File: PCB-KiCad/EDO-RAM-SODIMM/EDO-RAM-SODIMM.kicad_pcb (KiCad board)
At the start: 2 copper layers, 1 part

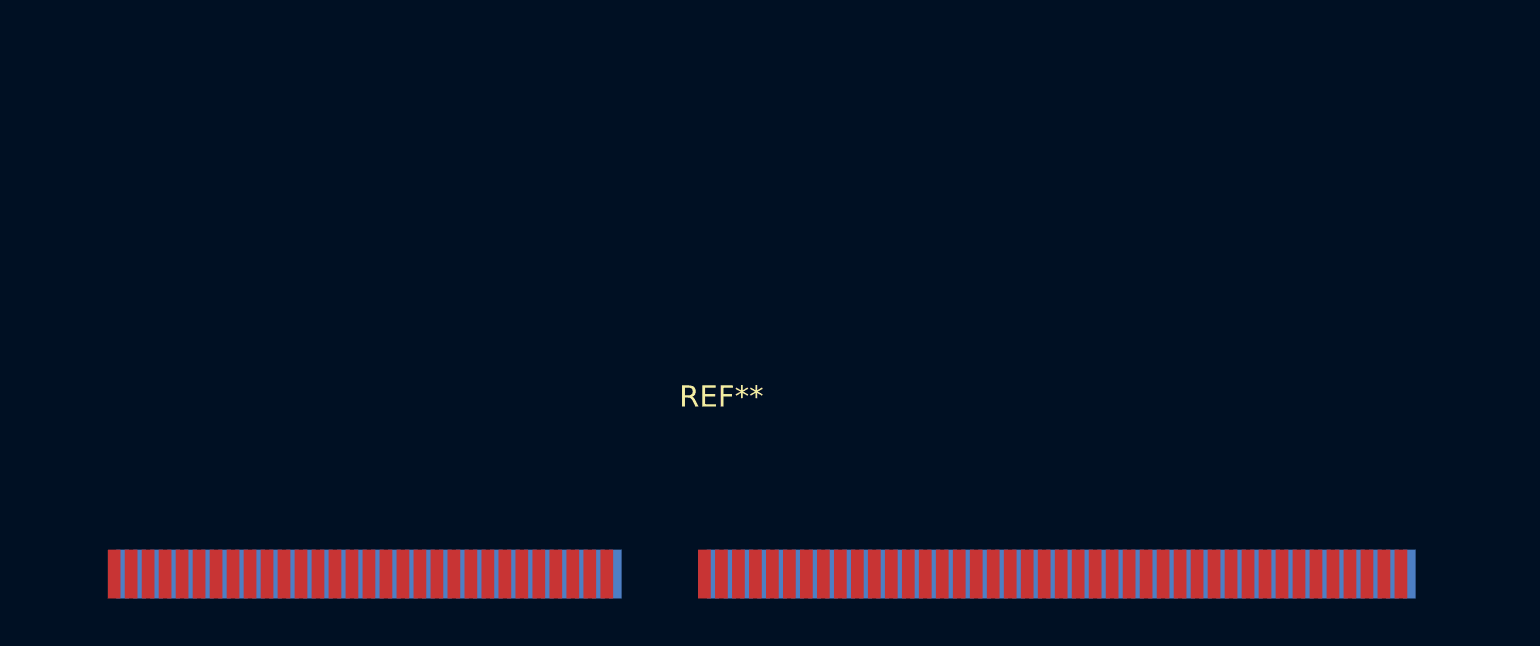
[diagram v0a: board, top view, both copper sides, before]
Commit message: U1 Connections
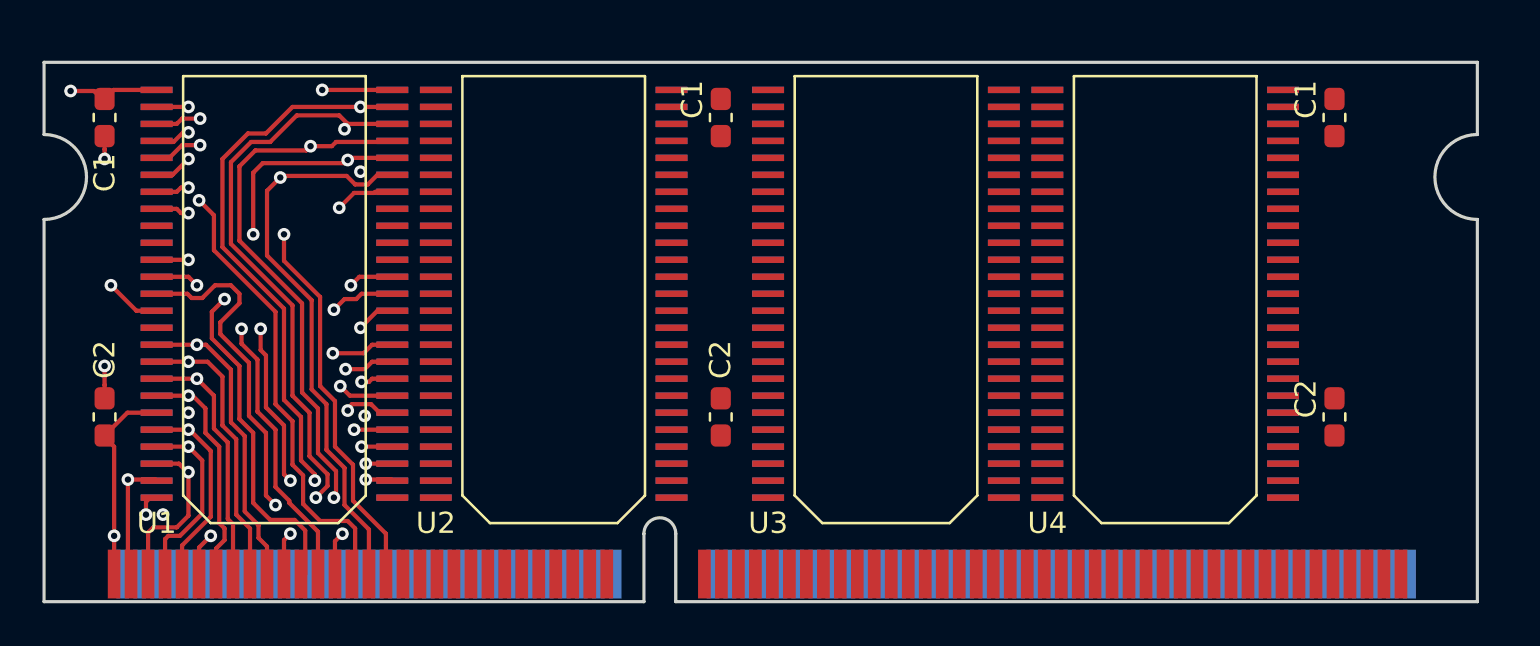
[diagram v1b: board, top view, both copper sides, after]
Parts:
- added C1: C_0603_1608Metric_Pad1.05x0.95mm_HandSolder, Capacitor_SMD:C_0603_1608Metric_Pad1.05x0.95mm_HandSolder, F.Cu at (150.4, 84.8)
- added C1: C_0603_1608Metric_Pad1.05x0.95mm_HandSolder, Capacitor_SMD:C_0603_1608Metric_Pad1.05x0.95mm_HandSolder, F.Cu at (121.5, 84.8)
- added C1: C_0603_1608Metric_Pad1.05x0.95mm_HandSolder, Capacitor_SMD:C_0603_1608Metric_Pad1.05x0.95mm_HandSolder, F.Cu at (92.5, 84.8)
- added C2: C_0603_1608Metric_Pad1.05x0.95mm_HandSolder, Capacitor_SMD:C_0603_1608Metric_Pad1.05x0.95mm_HandSolder, F.Cu at (150.4, 98.8)
- added C2: C_0603_1608Metric_Pad1.05x0.95mm_HandSolder, Capacitor_SMD:C_0603_1608Metric_Pad1.05x0.95mm_HandSolder, F.Cu at (121.5, 98.8)
- added C2: C_0603_1608Metric_Pad1.05x0.95mm_HandSolder, Capacitor_SMD:C_0603_1608Metric_Pad1.05x0.95mm_HandSolder, F.Cu at (92.5, 98.8)
- added U1: SOIC-50, obsolete-chips:SOIC-50, B.Cu at (100.7, 93.0)
- added U1: SOIC-50, obsolete-chips:SOIC-50, F.Cu at (100.7, 93.0)
- added U2: SOIC-50, obsolete-chips:SOIC-50, B.Cu at (113.8, 93.0)
- added U2: SOIC-50, obsolete-chips:SOIC-50, F.Cu at (113.8, 93.0)
- added U3: SOIC-50, obsolete-chips:SOIC-50, B.Cu at (129.5, 93.0)
- added U3: SOIC-50, obsolete-chips:SOIC-50, F.Cu at (129.5, 93.0)
- added U4: SOIC-50, obsolete-chips:SOIC-50, B.Cu at (142.7, 93.0)
- added U4: SOIC-50, obsolete-chips:SOIC-50, F.Cu at (142.7, 93.0)
- renumbered REF** to CN1
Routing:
- net (no net): track 0.00 -> 361.7 mm, vias 0 -> 60
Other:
- board outline added: 67.5 x 25.4 mm
- rule via_min_drill: 0.3 -> 0.1
- rule via_min_size: 0.4 -> 0.2

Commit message: Back Side Left IC Wiring (WIP).
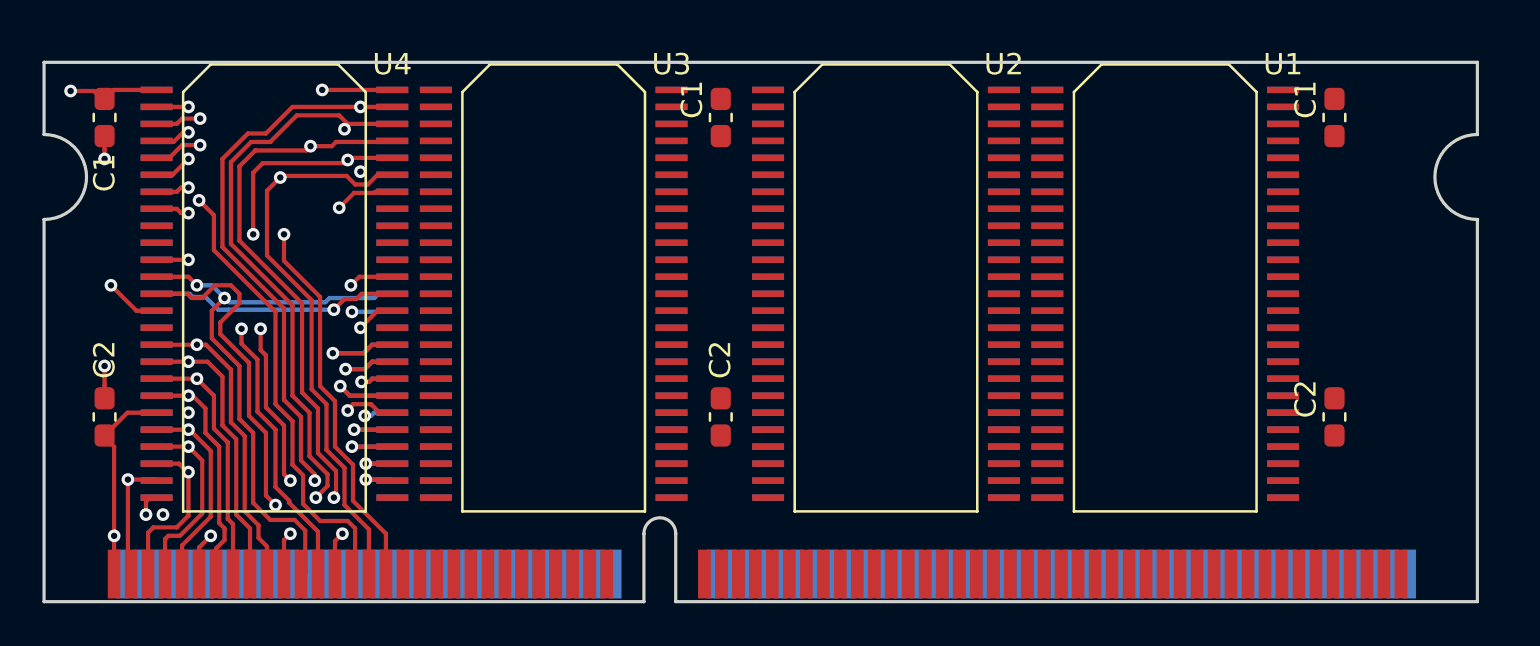
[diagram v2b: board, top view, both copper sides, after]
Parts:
- moved U4 42.4 mm to (100.3, 93.0), turned to 90 degrees
- moved U4 42.4 mm to (100.3, 93.0), turned to 270 degrees
- moved U1 41.5 mm to (142.2, 93.0), turned to 90 degrees
- moved U1 41.5 mm to (142.2, 93.0), turned to 270 degrees
- moved U3 16.0 mm to (113.5, 93.0), turned to 90 degrees
- moved U3 16.0 mm to (113.5, 93.0), turned to 270 degrees
- moved U2 15.2 mm to (129.1, 93.0), turned to 90 degrees
- moved U2 15.2 mm to (129.1, 93.0), turned to 270 degrees
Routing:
- net (no net): track 361.7 -> 399.4 mm, vias 60 -> 61
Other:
- net class Default: clearance 0.2 -> 0.13; trace_width 0.25 -> 0.15
- rule trace_clearance: 0.2 -> 0.13
- rule trace_min: 0.2 -> 0.15

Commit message: Fixed IC Positions.
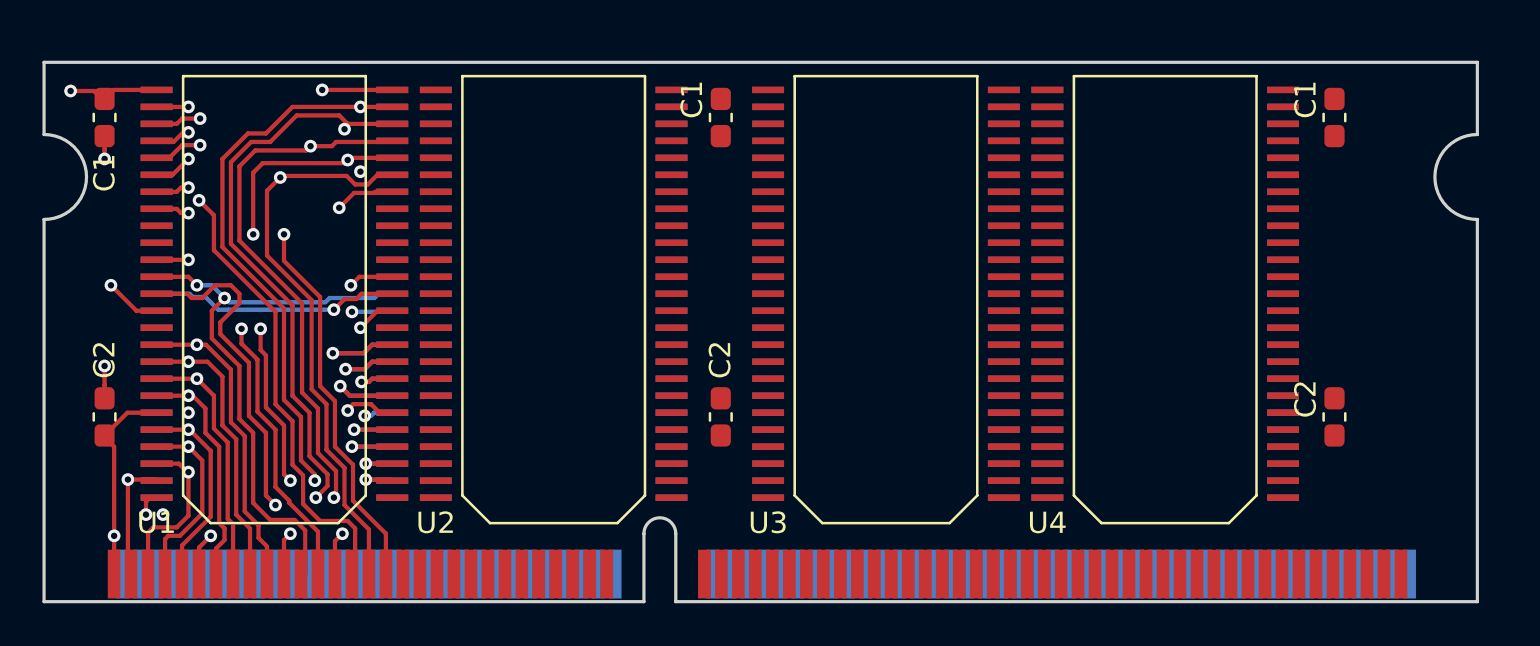
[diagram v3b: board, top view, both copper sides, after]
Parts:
- moved U4 42.4 mm to (142.7, 93.0), turned to 90 degrees
- moved U1 41.5 mm to (100.7, 93.0), turned to 90 degrees
- moved U3 16.0 mm to (129.5, 93.0), turned to 90 degrees
- moved U2 15.2 mm to (113.8, 93.0), turned to 90 degrees

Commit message: Surface layer Third IC F/B Complete
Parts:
- moved C2 2.55 mm to (121.5, 101.4)
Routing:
- net (no net): track 399.4 -> 1586.6 mm, vias 61 -> 217

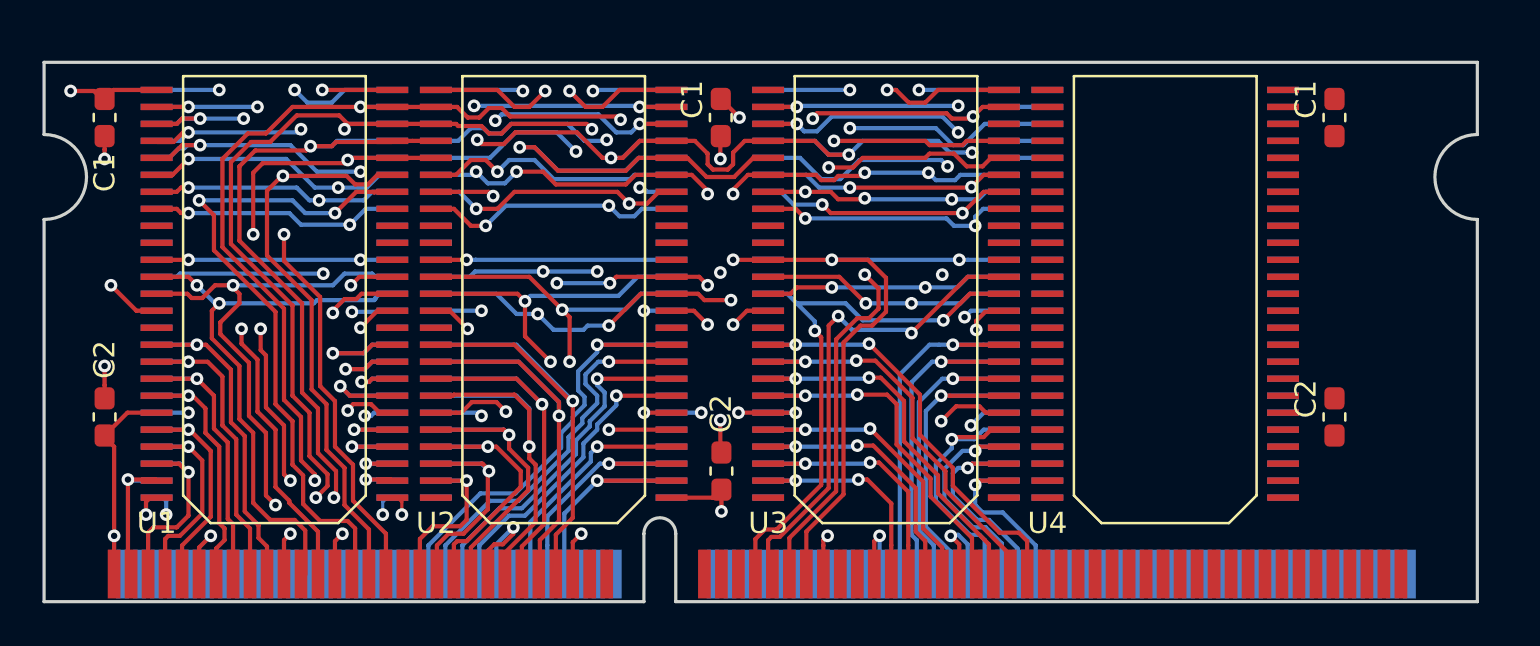
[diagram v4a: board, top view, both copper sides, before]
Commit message: Added caps and SPD ROM.
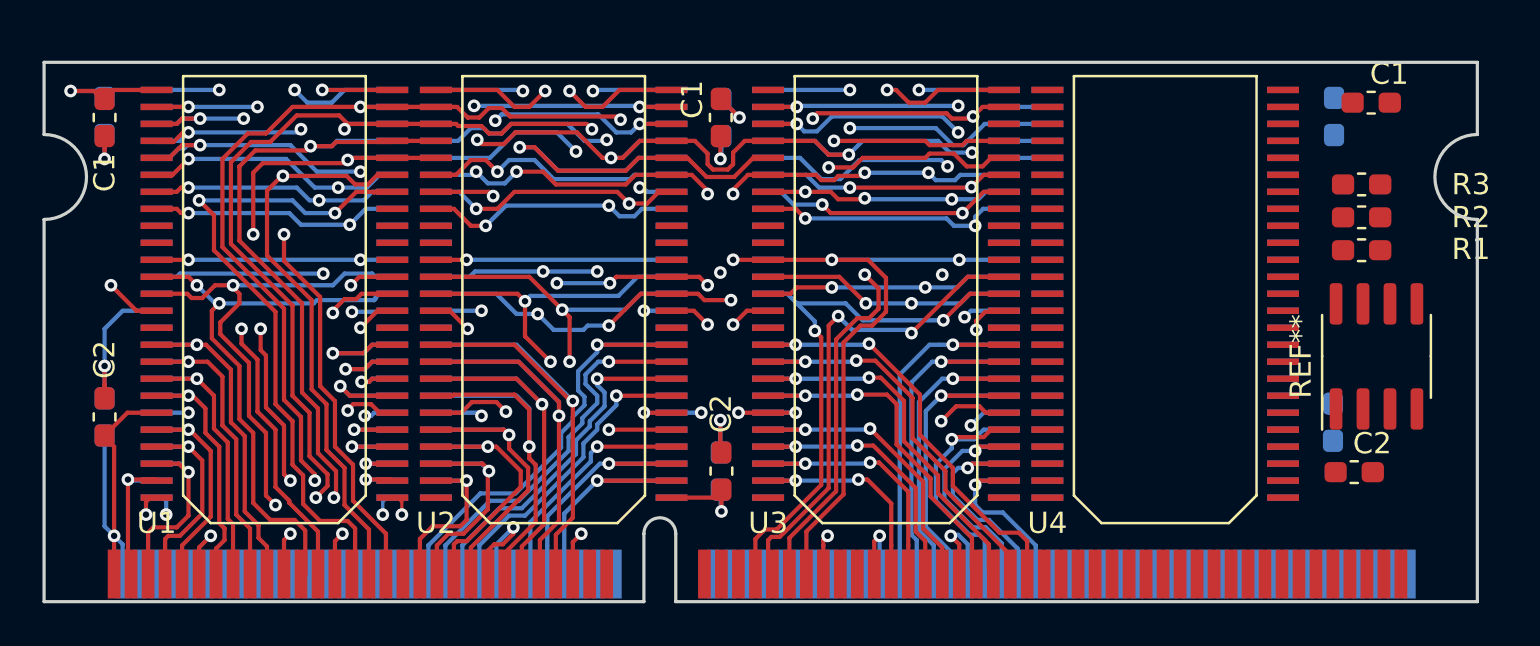
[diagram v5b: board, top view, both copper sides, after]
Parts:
- removed the C1 at (150.4, 84.8)
- removed the C2 at (150.4, 98.8)
- added C1: C_0603_1608Metric_Pad1.05x0.95mm_HandSolder, Capacitor_SMD:C_0603_1608Metric_Pad1.05x0.95mm_HandSolder, B.Cu at (150.3, 99.1)
- added C1: C_0603_1608Metric_Pad1.05x0.95mm_HandSolder, Capacitor_SMD:C_0603_1608Metric_Pad1.05x0.95mm_HandSolder, B.Cu at (92.5, 98.8)
- added C1: C_0603_1608Metric_Pad1.05x0.95mm_HandSolder, Capacitor_SMD:C_0603_1608Metric_Pad1.05x0.95mm_HandSolder, B.Cu at (121.5, 101.4)
- added C1: C_0603_1608Metric_Pad1.05x0.95mm_HandSolder, Capacitor_SMD:C_0603_1608Metric_Pad1.05x0.95mm_HandSolder, F.Cu at (152.2, 84.0)
- added C2: C_0603_1608Metric_Pad1.05x0.95mm_HandSolder, Capacitor_SMD:C_0603_1608Metric_Pad1.05x0.95mm_HandSolder, B.Cu at (150.4, 84.7)
- added C2: C_0603_1608Metric_Pad1.05x0.95mm_HandSolder, Capacitor_SMD:C_0603_1608Metric_Pad1.05x0.95mm_HandSolder, B.Cu at (92.5, 84.7)
- added C2: C_0603_1608Metric_Pad1.05x0.95mm_HandSolder, Capacitor_SMD:C_0603_1608Metric_Pad1.05x0.95mm_HandSolder, B.Cu at (121.5, 84.8)
- added C2: C_0603_1608Metric_Pad1.05x0.95mm_HandSolder, Capacitor_SMD:C_0603_1608Metric_Pad1.05x0.95mm_HandSolder, F.Cu at (151.3, 101.5)
- added R1: R_0603_1608Metric_Pad1.05x0.95mm_HandSolder, Resistor_SMD:R_0603_1608Metric_Pad1.05x0.95mm_HandSolder, F.Cu at (151.7, 91.0)
- added R2: R_0603_1608Metric_Pad1.05x0.95mm_HandSolder, Resistor_SMD:R_0603_1608Metric_Pad1.05x0.95mm_HandSolder, F.Cu at (151.7, 89.5)
- added R3: R_0603_1608Metric_Pad1.05x0.95mm_HandSolder, Resistor_SMD:R_0603_1608Metric_Pad1.05x0.95mm_HandSolder, F.Cu at (151.7, 87.9)
- added REF**: SOIC-8_3.9x4.9mm_P1.27mm, Package_SO:SOIC-8_3.9x4.9mm_P1.27mm, F.Cu at (152.4, 96.0)
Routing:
- net (no net): track 1586.6 -> 1607.3 mm
